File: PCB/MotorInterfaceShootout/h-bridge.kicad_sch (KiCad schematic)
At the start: 47 parts, among them U5 74LS14, U6 74LS08

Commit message: fix power
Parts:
- removed D? (x3): Red, symbol Drivers-rescue:LED-00TJR
- removed D? (x3): Green, symbol Drivers-rescue:LED-00TJR
- removed Q? (x2): Reverse, Package_TO_SOT_THT:TO-92_Inline, symbol Drivers-rescue:NEMOSFET-00TJR
- removed Q? (x2): Forward, Package_TO_SOT_THT:TO-92_Inline, symbol Drivers-rescue:NEMOSFET-00TJR
- removed Q? (x2): Forward, Package_TO_SOT_THT:TO-92_Inline, symbol Drivers-rescue:PEMOSFET-00TJR
- removed Q? (x2): Reverse, Package_TO_SOT_THT:TO-92_Inline, symbol Drivers-rescue:PEMOSFET-00TJR
- removed R? (x6): R_US, symbol Device:R_US
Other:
- note removed: "Dual MOSFET Single Direction"
- note removed: "Individual MOSFET Drivers"

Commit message: working on h-bridge logic
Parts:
- removed R? (x11): 330, symbol Device:R_US
- removed U? (x4): Optocoupler, symbol Drivers-rescue:Optocoupler-Device
- added Q1, Q2, Q3, Q4: 2N3904, TO-92, symbol TJR:2N3904
- added R10, R2, R3, R4, R7, R8, R9: 10k, symbol Device:R_US
- added U10, U11, U8, U9: 74LS32, symbol 74xx:74LS32
- R?: value 330 -> 10k
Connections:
- net F1iso: now also Q2.~ (E), R4.1
- net R1iso: now also Q4.~ (E), R10.1
- net ~{F0iso}: now also Q1.~ (E)
- net ~{Forward0}: now also Q1.~ (E)
- net ~{Forward1}: now also Q2.~ (E)
- net ~{R0iso}: now also Q3.~ (E), R7.2
- net ~{Reverse0}: now also Q3.~ (E)
- net ~{Reverse1}: now also Q4.~ (E)
- net at U6.2: no longer U5.2
- net at U6.3: no longer U6.5
- net at U6.10: no longer U5.10
- net at U6.8: no longer U5.9
- net at U6.9: no longer U6.11
- net at U5.4: no longer U6.4
- net at U5.12: no longer U6.12
- net at U5.5: no longer U6.6
- removed net A: U5.1, U5.11, U6.1
- removed net B: U5.13, U5.3, U6.13
- net GNDS renamed GND
- net GND: now also R10.2, R2.2, R4.2, R8.2
- net Vdrive renamed VSYS
- net VSYS: now also R3.1, R7.1, R9.1
- net ~{Decrement}: no longer names the net of U5.8
- net ~{Increment}: no longer names the net of U5.6
- new net: Q4.~ (E), R9.2
- new net: Q3.~ (E), R8.1
- new net: Q1.~ (E), R2.1
- new net: Q2.~ (E), R3.2
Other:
- note removed: "Encoder State Detectors & Pulse Generators"
- moved on the sheet: U5A, U5B, U5C, U5D, U5E, U5F, U6A, U6B, U6C, U6D

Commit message: fix h-bridge pwm logic
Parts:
- removed U10, U11, U8, U9: 74LS32, symbol 74xx:74LS32
- removed U5: 74LS14, symbol S2020-cache:74xx_74LS14
- removed U6: 74LS08, symbol TFlipFlop-cache:74xx_74LS08
- added D8: Red, symbol Drivers-rescue:LED-00TJR
- added JP2: Jumper_2_Open, symbol jumper:Jumper_2_Open
- added R11: 10k, symbol Device:R_US
- added U13, U7, U8: 74LS08, symbol TFlipFlop-cache:74xx_74LS08
- added U6: 74LS14, symbol S2020-cache:74xx_74LS14
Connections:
- net GND: now also D8.1 (K); no longer R2.2
- net ~{Forward0}: now also U13.3, U6.11, U6.13
- net ~{Forward1}: now also U7.3
- net ~{Reverse0}: now also U13.11, U7.1, U8.2
- net ~{Reverse1}: now also U8.3
- new net: U6.12, U7.2
- new net: JP2.2 (B), R11.2, U13.1, U13.13
- new net: D8.2 (A), R2.2
- new net: U6.10, U8.1
- new net +5V: R11.1
- new net PIN_PWM_SPD_CMD: JP2.1 (A)
- new net S0: U13.2
- new net S1: U13.12

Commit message: change MOSFET/LED drivers to MOSFET to keep ttl in spec
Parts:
- removed D?: Red, symbol Drivers-rescue:LED-00TJR
- removed D?: Green, symbol Drivers-rescue:LED-00TJR
- removed M?: Motor_DC, symbol 00TJR:Motor_DC
- removed Q1, Q2, Q3, Q4: 2N3904, TO-92, symbol TJR:2N3904
- removed Q?: Forward, Package_TO_SOT_THT:TO-92_Inline, symbol Drivers-rescue:NEMOSFET-00TJR
- removed Q?: Reverse, Package_TO_SOT_THT:TO-92_Inline, symbol Drivers-rescue:PEMOSFET-00TJR
- removed R10, R7, R8, R9, R?: 10k, symbol Device:R_US
- removed R? (x2): R_US, symbol Device:R_US
- added C7: 0.1uF, TJR:C_Radial_D5.00mm_H12.5mm_P2.00mm, symbol device:C
- added D10: Red, symbol Drivers-rescue:LED-00TJR
- added D11, D9: Green, symbol Drivers-rescue:LED-00TJR
- added Q1, Q2, Q3, Q4: 2N7002, symbol Drivers-rescue:NEMOSFET-00TJR
- added Q5: G20N03K, symbol Drivers-rescue:NEMOSFET-00TJR
- added Q6: G160P03KI, symbol Drivers-rescue:PEMOSFET-00TJR
- added R13: 680, symbol Device:R_US
- added R7, R8: 1.3k, TJR:R_Axial_DIN0207_L6.3mm_D2.5mm_P7.62mm_Horizontal, symbol TJR:R
- Q?: value Reverse -> G20N03K; footprint Package_TO_SOT_THT:TO-92_Inline -> (none); digikey (none) -> https://www.digikey.com/en/products/detail/goford-semicondu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
- Q?: value Forward -> G160P03KI; footprint Package_TO_SOT_THT:TO-92_Inline -> (none); digikey (none) -> https://www.digikey.com/en/products/detail/goford-semicondu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
- R2, R3, R4: value 10k -> 680
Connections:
- net ~{Forward1} is gone; now on net F1iso: U7.3
- net ~{Reverse1} is gone; now on net R1iso: U8.3
- net F1iso: now also Q4.2 (G), Q5.2 (G); no longer R4.1
- net GND: now also D9.1 (K), Q1.3 (S), Q3.3 (S), Q5.3 (S); no longer R4.2
- net M+: now also Q?.1 (D), Q?.3 (D), C7.1
- net M-: now also C7.2, Q5.1 (D), Q6.3 (D)
- net R1iso: now also Q2.2 (G)
- net VSYS: now also Q6.1 (S), R13.1, R7.1, R8.1
- net ~{F0iso}: now also R2.1, R13.2
- net ~{R0iso}: now also R3.2, R4.1, Q6.2 (G)
- net at D8.2 (A): now also Q2.3 (S); no longer R2.2
- net ~{Forward0} renamed Forward0
- net Forward0: now also Q1.2 (G)
- net ~{Reverse0} renamed Reverse0
- net Reverse0: now also Q3.2 (G)
- new net: Q2.1 (D), R7.2
- new net: D11.2 (A), R2.2
- new net: Q4.1 (D), R8.2
- new net: D9.2 (A), Q4.3 (S)
- new net: D10.1 (K), Q3.1 (D)
- new net: D10.2 (A), R4.2
- new net: D11.1 (K), Q1.1 (D)
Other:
- note removed: "Final H-Bridge"
- note removed: "Note: Vdrive and Isolated ground are electircally Isolated from the digital control circuitry. Resistor values must be determined based on specific implementation."
- note removed: "Optical Isolation"
- moved on the sheet: JP2, R11, R2, U13A, U13D, U6E, U6F, U7A, U8A

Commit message: working on part source
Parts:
- C10: renamed from C7; footprint TJR:C_Radial_D5.00mm_H12.5mm_P2.00mm -> (none); digikey https://www.digikey.com/en/products/detail/rubycon/16ZLH100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 -> https://www.digikey.com/en/products/detail/cal-chip-electro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
- D10: renamed from D11; digikey (none) -> https://www.digikey.com/en/products/detail/ams-osram-usa-in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
- D11: renamed from D8; digikey (none) -> https://www.digikey.com/en/products/detail/ams-osram-usa-in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
- D12: renamed from D10; digikey (none) -> https://www.digikey.com/en/products/detail/ams-osram-usa-in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
- D13: renamed from D9; digikey (none) -> https://www.digikey.com/en/products/detail/ams-osram-usa-in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
- R19: renamed from R7; value 1.3k -> 1.3kx; footprint TJR:R_Axial_DIN0207_L6.3mm_D2.5mm_P7.62mm_Horizontal -> (none)
- R20: renamed from R11; digikey (none) -> https://www.digikey.com/en/products/detail/stackpole-electr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
- R23: renamed from R8; value 1.3k -> 1.3kx; footprint TJR:R_Axial_DIN0207_L6.3mm_D2.5mm_P7.62mm_Horizontal -> (none)
- U5: renamed from U6; digikey (none) -> https://www.digikey.com/en/products/detail/texas-instrument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
- U6: renamed from U7; digikey (none) -> https://www.digikey.com/en/products/detail/texas-instrument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
- U6: renamed from U13; digikey (none) -> https://www.digikey.com/en/products/detail/texas-instrument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
- U6: renamed from U8; digikey (none) -> https://www.digikey.com/en/products/detail/texas-instrument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
- gave numbers to parts that had none: 2
- renumbered Q6 to Q7, Q5 to Q8, R13 to R17, R2 to R18, R3 to R21, R4 to R22
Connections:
- net F1iso: now also U6.8; no longer U6.3
- net GND: now also Q2.3 (S), Q4.3 (S); no longer D11.1 (K), D13.1 (K)
- net R1iso: now also U6.11; no longer U6.3
- net Reverse0: now also U6.13, U6.6, U6.9; no longer U6.1, U6.11, U6.2
- net S1: now also U6.4; no longer U6.12
- net at U5.12: now also U6.10; no longer U6.2
- net at Q2.1 (D): now also D11.1 (K); no longer R19.2
- net at D11.2 (A): now also R19.2; no longer Q2.3 (S)
- net at JP2.2 (B), R20.2, U6.1: now also U6.5; no longer U6.13
- net at U5.10: now also U6.12; no longer U6.1
- net at Q4.1 (D): now also D13.1 (K); no longer R23.2
- net at D13.2 (A): now also R23.2; no longer Q4.3 (S)
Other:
- moved on the sheet: C10, Q2, Q4, Q5, Q6, Q7, Q8

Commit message: commit before schema change
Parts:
- JP2: digikey (none) -> https://www.digikey.com/en/products/detail/sullins-connecto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
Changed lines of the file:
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@@
 			)
 		)
-		(property "Datasheet" "~"
+		(property "Datasheet" "https://s3.amazonaws.com/catalogspreads-pdf/PAGE128-129%20.100%20JUMPER.pdf"
 			(at 59.69 48.26 0)
 			(effects
@@
 			)
 		)
-		(property "Description" ""
+		(property "Description" "CONN JUMPER SHORTING .100\" GOLD"
 			(at 59.69 48.26 0)
 			(effects
+				(font
+					(size 1.27 1.27)
+				)
+				(hide yes)
+			)
+		)
+		(property "digikey" "https://www.digikey.com/en/products/detail/sullins-connector-solutions/QPC02SXGN-RC/2618262"
+			(at 59.69 48.26 0)
+			(effects

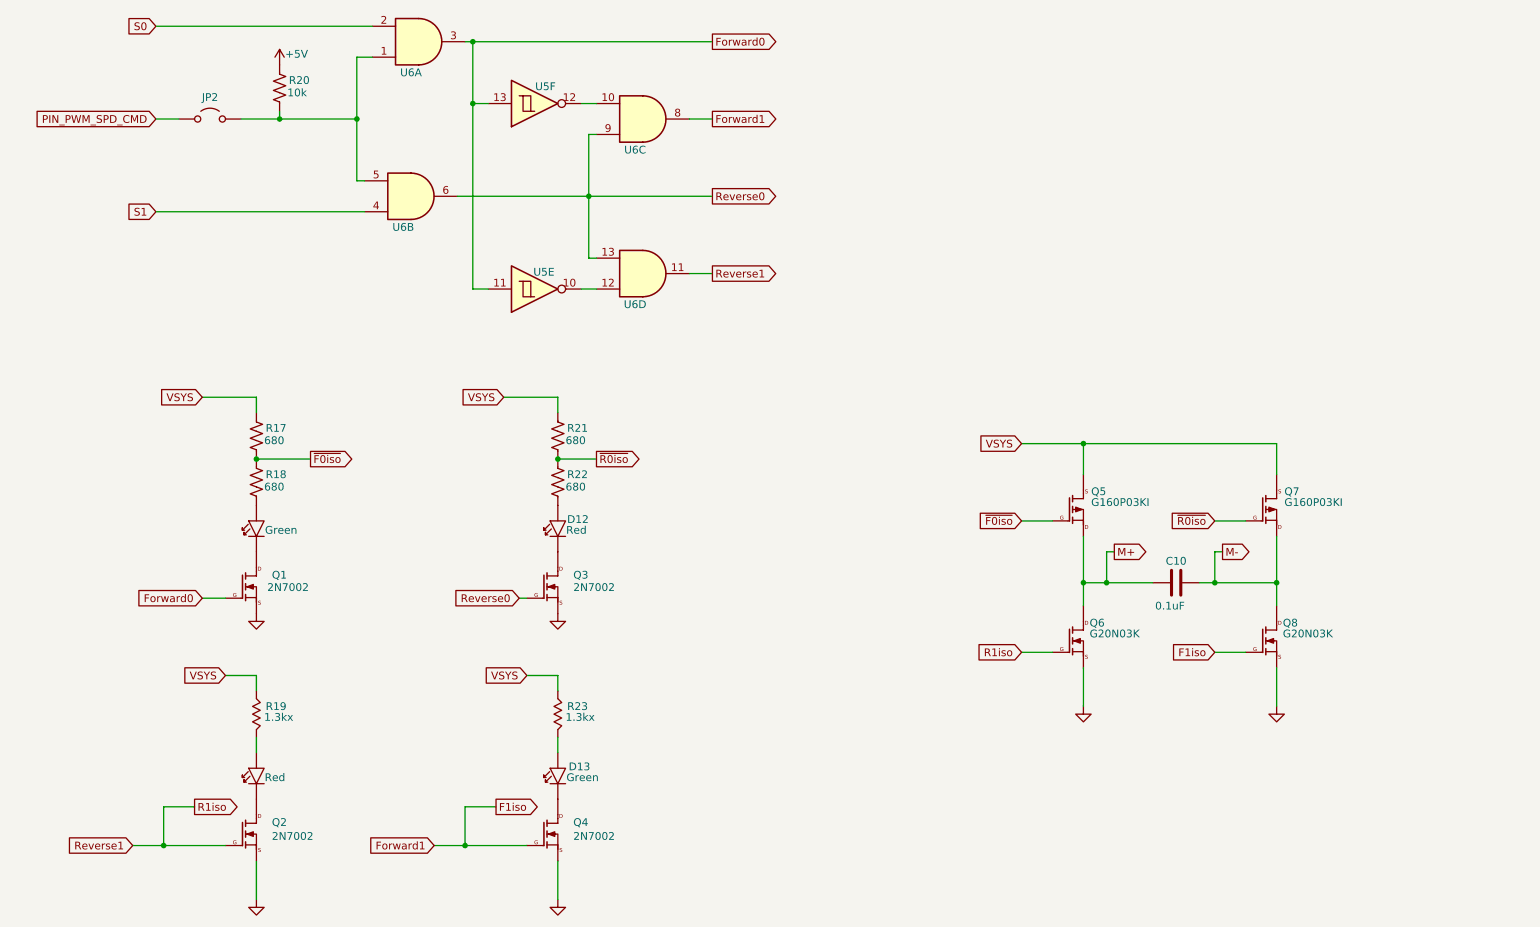
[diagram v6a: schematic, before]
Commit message: new h-bridge config
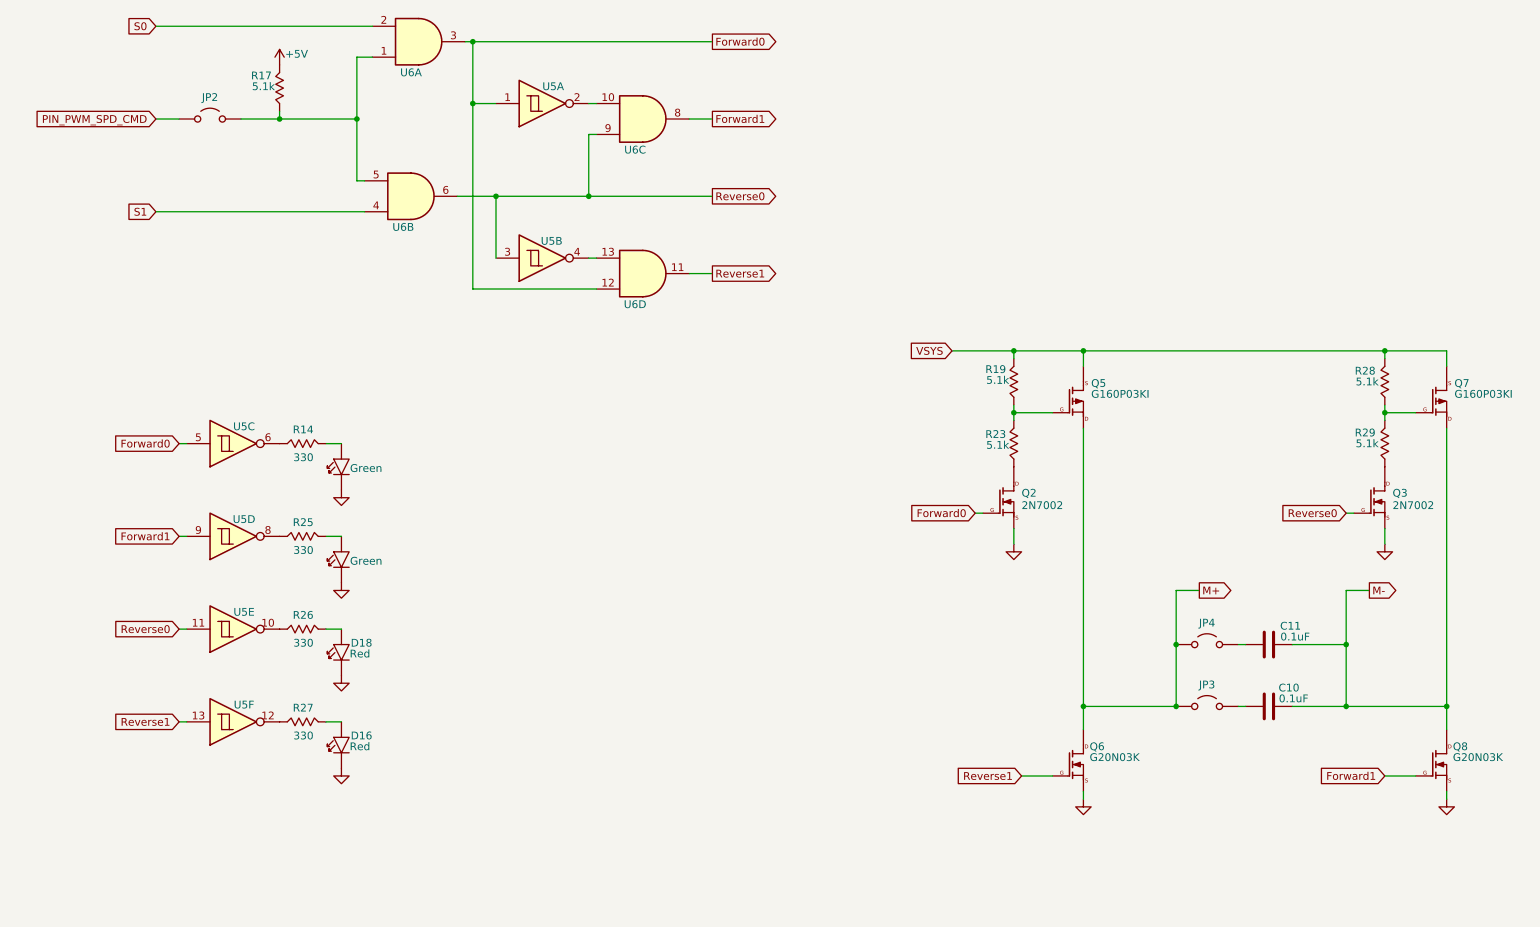
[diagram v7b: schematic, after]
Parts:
- removed D10, D13: Green, symbol Drivers-rescue:LED-00TJR
- removed D11, D12: Red, symbol Drivers-rescue:LED-00TJR
- removed Q1, Q4: 2N7002, symbol Drivers-rescue:NEMOSFET-00TJR
- removed R17, R18, R21, R22: 680, symbol Device:R_US
- removed R20: 10k, symbol Device:R_US
- added C11: 0.1uF, symbol device:C
- added D14, D15: Green, symbol Drivers-rescue:LED-00TJR
- added D16, D18: Red, symbol Drivers-rescue:LED-00TJR
- added JP3, JP4: Jumper_2_Open, symbol jumper:Jumper_2_Open
- added R14, R25, R26, R27: 330, symbol TJR:R
- added R17, R28, R29: 5.1k, symbol TJR:R
- added unit 6 of U5
- added unit 3 of U5
- added unit 4 of U5
- added unit 5 of U5
- R19, R23: value 1.3kx -> 5.1k; digikey https://www.digikey.com/en/products/detail/stackpole-electronics-inc/RNCP1206FTD1K30/2240340 -> https://www.digikey.com/en/products/detail/stackpole-electronics-inc/RMEF0805FT5K10/16839706
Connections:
- net ~{F0iso} is gone; now on an unnamed net: Q5.2 (G)
- net +5V: now also R17.2
- net Forward0: now also Q2.2 (G), U5.1, U6.12, U5.5; no longer U5.11, U5.13
- net GND: now also D14.1 (K), D15.1 (K), D16.1 (K), D18.1 (K)
- net M+: now also JP3.1 (A), JP4.1 (A); no longer C10.1
- net M-: now also C11.2
- net Reverse0: now also U5.3, U5.11; no longer U6.13
- net VSYS: now also R19.2, R28.2; no longer R19.1, R23.1
- net at U6.10: now also U5.2; no longer U5.12
- net at Q2.1 (D): now also R23.1
- net at JP2.2 (B), U6.1, U6.5: now also R17.1
- net at R23.2: now also R19.1
- net at Q3.1 (D): now also R29.1
- net F1iso renamed Forward1
- net Forward1: now also U5.9
- net R1iso renamed Reverse1
- net Reverse1: now also U5.13; no longer Q2.2 (G)
- net ~{R0iso}: no longer names the net of Q7.2 (G)
- net ~{R0iso}: now also R28.1, R29.2
- new net: R27.1, U5.12
- new net: D18.2 (A), R26.2
- new net: U5.4, U6.13
- new net: R14.1, U5.6
- new net: D14.2 (A), R14.2
- new net: C11.1, JP4.2 (B)
- new net: D15.2 (A), R25.2
- new net: D16.2 (A), R27.2
- new net: C10.1, JP3.2 (B)
- new net: R25.1, U5.8
- new net: R26.1, U5.10
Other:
- moved on the sheet: C10, Q3, Q5, Q6, Q7, Q8, U5A, U5B

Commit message: most footprints, added and measured/confirmed
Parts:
- C10, C11: footprint (none) -> C_SMD:C_0805_2012Metric
- D14, D15, D16, D18: footprint (none) -> LED_SMD:LED_0805_2012Metric_Pad1.15x1.40mm_HandSolder
- Q2, Q3: footprint (none) -> TO_SOT_SMD:SOT-23
- R14, R17, R19, R23, R25, R26, R27, R28, R29: footprint (none) -> R_SMD:R_0805_2012Metric
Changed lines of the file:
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@@
 			)
 		)
-		(property "Footprint" ""
+		(property "Footprint" "LED_SMD:LED_0805_2012Metric_Pad1.15x1.40mm_HandSolder"
 			(at 81.28 135.89 90)
 			(effects
@@
 			)
 		)
-		(property "Footprint" ""
+		(property "Footprint" "TO_SOT_SMD:SOT-23"
 			(at 195.58 114.935 0)
 			(effects
@@
 			)
 		)
-		(property "Footprint" ""
+		(property "Footprint" "R_SMD:R_0805_2012Metric"
 			(at 254.508 91.44 90)
 			(effects
@@
 			)
 		)
-		(property "Footprint" ""
+		(property "Footprint" "LED_SMD:LED_0805_2012Metric_Pad1.15x1.40mm_HandSolder"
 			(at 81.28 105.41 90)
 			(effects
@@
 			)
 		)
-		(property "Footprint" ""
+		(property "Footprint" "R_SMD:R_0805_2012Metric"
 			(at 193.548 101.6 90)
 			(effects
@@
 			)
 		)
-		(property "Footprint" ""
+		(property "Footprint" "LED_SMD:LED_0805_2012Metric_Pad1.15x1.40mm_HandSolder"
 			(at 81.28 120.65 90)
 			(effects
@@
 			)
 		)
-		(property "Footprint" ""
+		(property "Footprint" "R_SMD:R_0805_2012Metric"
 			(at 74.93 149.098 90)
 			(effects
@@
 			)
 		)
-		(property "Footprint" ""
+		(property "Footprint" "R_SMD:R_0805_2012Metric"
 			(at 254.508 101.6 90)
 			(effects
@@
 			)
 		)
-		(property "Footprint" ""
+		(property "Footprint" "C_SMD:C_0805_2012Metric"
 			(at 237.49 133.6548 0)
 			(effects
@@
 			)
 		)
-		(property "Footprint" ""
+		(property "Footprint" "C_SMD:C_0805_2012Metric"
 			(at 237.49 143.8148 0)
 			(effects
@@
 			)
 		)
-		(property "Footprint" ""
+		(property "Footprint" "LED_SMD:LED_0805_2012Metric_Pad1.15x1.40mm_HandSolder"
 			(at 81.28 151.13 90)
 			(effects
@@
 			)
 		)
-		(property "Footprint" ""
+		(property "Footprint" "R_SMD:R_0805_2012Metric"
 			(at 74.93 103.378 90)
 			(effects
@@
 			)
 		)
-		(property "Footprint" ""
+		(property "Footprint" "R_SMD:R_0805_2012Metric"
 			(at 74.93 118.618 90)
 			(effects
@@
 			)
 		)
-		(property "Footprint" ""
+		(property "Footprint" "R_SMD:R_0805_2012Metric"
 			(at 74.93 133.858 90)
 			(effects
@@
 			)
 		)
-		(property "Footprint" ""
+		(property "Footprint" "R_SMD:R_0805_2012Metric"
 			(at 72.898 43.18 90)
 			(effects
@@
 			)
 		)
-		(property "Footprint" ""
+		(property "Footprint" "TO_SOT_SMD:SOT-23"
 			(at 256.54 114.935 0)
 			(effects
@@
 			)
 		)
-		(property "Footprint" ""
+		(property "Footprint" "R_SMD:R_0805_2012Metric"
 			(at 193.548 91.44 90)
 			(effects
